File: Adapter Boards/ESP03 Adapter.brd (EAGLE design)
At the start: 30.1 x 19 mm, 3 parts, among them U1 ESP03

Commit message: Added OSHW logos
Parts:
- added LOGO1: OSHW-LOGOM, SparkFun-Aesthetics:OSHW-LOGO-M
- renumbered JP1 to 1, JP2 to 2
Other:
- board size 30.1 x 19 mm -> 30.1 x 19.7 mm
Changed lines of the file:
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@@
 <plain>
 <wire x1="0" y1="0" x2="30.15" y2="0" width="0" layer="20"/>
-<wire x1="30.15" y1="0" x2="30.15" y2="19.04" width="0" layer="20"/>
-<wire x1="30.15" y1="19.04" x2="0" y2="19.04" width="0" layer="20"/>
-<wire x1="0" y1="19.04" x2="0" y2="0" width="0" layer="20"/>
+<wire x1="30.15" y1="0" x2="30.15" y2="19.675" width="0" layer="20"/>
+<wire x1="30.15" y1="19.675" x2="0" y2="19.675" width="0" layer="20"/>
+<wire x1="0" y1="19.675" x2="0" y2="0" width="0" layer="20"/>
 </plain>
 <attributes>
@@
 </autorouter>
 <elements>
-<element name="JP1" library="SparkFun-Connectors" package="1X07" value="" x="1.905" y="1.905" rot="R90"/>
-<element name="JP2" library="SparkFun-Connectors" package="1X07" value="" x="28.575" y="1.905" rot="R90"/>
+<element name="1" library="SparkFun-Connectors" package="1X07" value="" x="1.905" y="1.905" smashed="yes" rot="R90">
+<attribute name="NAME" x="3.7338" y="0.7112" size="1.27" layer="27" ratio="10" rot="R270"/>
+<attribute name="VALUE" x="5.08" y="0.635" size="1.27" layer="27" rot="R90"/>
+</element>
+<element name="2" library="SparkFun-Connectors" package="1X07" value="" x="28.575" y="1.905" smashed="yes" rot="R90">
+<attribute name="NAME" x="26.7462" y="0.5588" size="1.27" layer="27" ratio="10" rot="R90"/>
+<attribute name="VALUE" x="31.75" y="0.635" size="1.27" layer="27" rot="R90"/>
+</element>
 <element name="U1" library="ESP" package="ESP03" value="ESP03" x="8.89" y="18.415"/>
+<element name="LOGO1" library="SparkFun-Aesthetics" package="OSHW-LOGO-M" value="OSHW-LOGOM" x="24.13" y="16.51"/>
 </elements>
 <signals>
 <signal name="N$1">
 <contactref element="U1" pad="VCC"/>
-<contactref element="JP1" pad="7"/>
+<contactref element="1" pad="7"/>
 <wire x1="9.09" y1="14.015" x2="5.035" y2="14.015" width="0.4064" layer="1"/>
 <wire x1="5.035" y1="14.015" x2="1.905" y2="17.145" width="0.4064" layer="1"/>
@@
 <signal name="N$2">
 <contactref element="U1" pad="GPIO14"/>
-<contactref element="JP1" pad="6"/>
+<contactref element="1" pad="6"/>
 <wire x1="9.09" y1="12.015" x2="4.495" y2="12.015" width="0.4064" layer="1"/>
 <wire x1="4.495" y1="12.015" x2="1.905" y2="14.605" width="0.4064" layer="1"/>
@@
 <signal name="N$3">
 <contactref element="U1" pad="GPIO12"/>
-<contactref element="JP1" pad="5"/>
+<contactref element="1" pad="5"/>
 <wire x1="9.09" y1="10.015" x2="3.955" y2="10.015" width="0.4064" layer="1"/>
 <wire x1="3.955" y1="10.015" x2="1.905" y2="12.065" width="0.4064" layer="1"/>
@@
 <signal name="N$4">
 <contactref element="U1" pad="GPIO13"/>
-<contactref element="JP1" pad="4"/>
+<contactref element="1" pad="4"/>
 <wire x1="9.09" y1="8.015" x2="3.415" y2="8.015" width="0.4064" layer="1"/>
 <wire x1="3.415" y1="8.015" x2="1.905" y2="9.525" width="0.4064" layer="1"/>
@@
 <signal name="N$5">
 <contactref element="U1" pad="GPIO15"/>
-<contactref element="JP1" pad="3"/>
+<contactref element="1" pad="3"/>
 <wire x1="9.09" y1="6.015" x2="2.875" y2="6.015" width="0.4064" layer="1"/>
 <wire x1="2.875" y1="6.015" x2="1.905" y2="6.985" width="0.4064" layer="1"/>
@@
 <signal name="N$6">
 <contactref element="U1" pad="GPIO2"/>
-<contactref element="JP1" pad="2"/>
+<contactref element="1" pad="2"/>
 <wire x1="9.09" y1="4.015" x2="2.335" y2="4.015" width="0.4064" layer="1"/>
 <wire x1="2.335" y1="4.015" x2="1.905" y2="4.445" width="0.4064" layer="1"/>
@@
 <signal name="N$7">
 <contactref element="U1" pad="GPIO0"/>
-<contactref element="JP1" pad="1"/>
+<contactref element="1" pad="1"/>
 <wire x1="9.09" y1="2.015" x2="2.015" y2="2.015" width="0.4064" layer="1"/>
 <wire x1="2.015" y1="2.015" x2="1.905" y2="1.905" width="0.4064" layer="1"/>
@@
 <signal name="N$8">
 <contactref element="U1" pad="ANT"/>
-<contactref element="JP2" pad="7"/>
+<contactref element="2" pad="7"/>
 <wire x1="20.69" y1="14.015" x2="25.445" y2="14.015" width="0.4064" layer="1"/>
 <wire x1="25.445" y1="14.015" x2="28.575" y2="17.145" width="0.4064" layer="1"/>
@@
 <signal name="N$9">
 <contactref element="U1" pad="CH_PD"/>
-<contactref element="JP2" pad="6"/>
+<contactref element="2" pad="6"/>
 <wire x1="20.69" y1="12.015" x2="25.985" y2="12.015" width="0.4064" layer="1"/>
 <wire x1="25.985" y1="12.015" x2="28.575" y2="14.605" width="0.4064" layer="1"/>
@@
 <signal name="N$10">
 <contactref element="U1" pad="GPIO18"/>
-<contactref element="JP2" pad="5"/>
+<contactref element="2" pad="5"/>
 <wire x1="20.69" y1="10.015" x2="26.525" y2="10.015" width="0.4064" layer="1"/>
 <wire x1="26.525" y1="10.015" x2="28.575" y2="12.065" width="0.4064" layer="1"/>
@@
 <signal name="N$11">
 <contactref element="U1" pad="URXD"/>
-<contactref element="JP2" pad="4"/>
+<contactref element="2" pad="4"/>
 <wire x1="20.69" y1="8.015" x2="27.065" y2="8.015" width="0.4064" layer="1"/>
 <wire x1="27.065" y1="8.015" x2="28.575" y2="9.525" width="0.4064" layer="1"/>
@@
 <signal name="N$12">
 <contactref element="U1" pad="UTXD"/>
-<contactref element="JP2" pad="3"/>
+<contactref element="2" pad="3"/>
 <wire x1="20.69" y1="6.015" x2="27.605" y2="6.015" width="0.4064" layer="1"/>
 <wire x1="27.605" y1="6.015" x2="28.575" y2="6.985" width="0.4064" layer="1"/>
@@
 <signal name="N$13">
 <contactref element="U1" pad="GND"/>
-<contactref element="JP2" pad="1"/>
+<contactref element="2" pad="1"/>
 <wire x1="20.69" y1="2.015" x2="28.465" y2="2.015" width="0.4064" layer="1"/>
 <wire x1="28.465" y1="2.015" x2="28.575" y2="1.905" width="0.4064" layer="1"/>

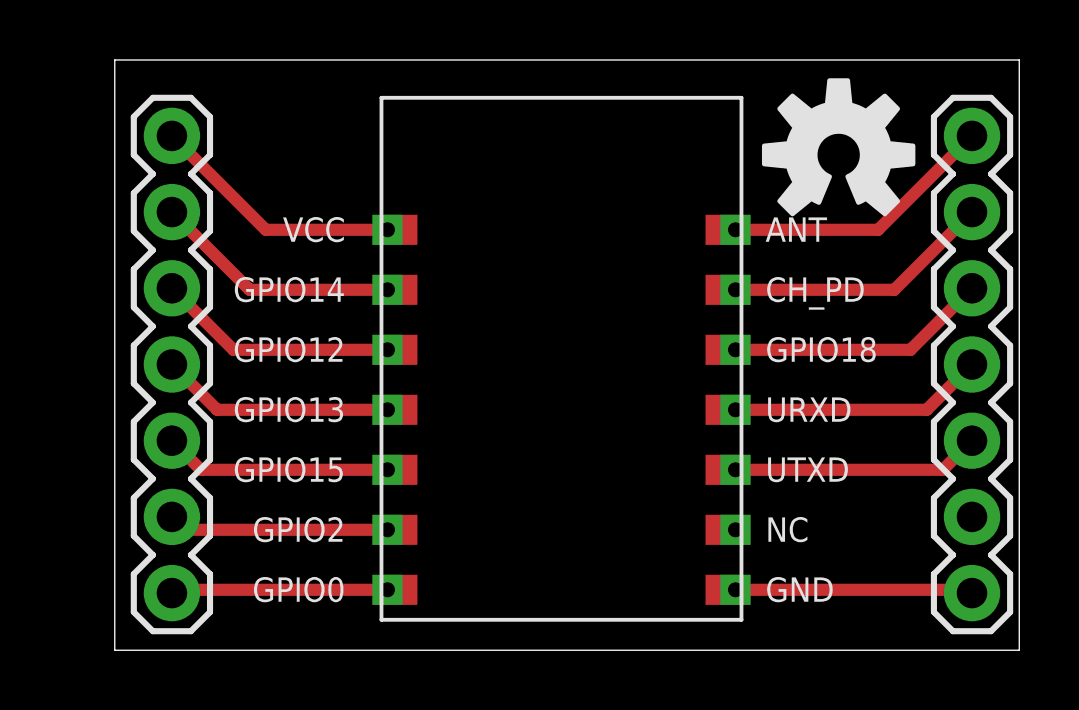
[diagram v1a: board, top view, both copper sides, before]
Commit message: Added hark logo
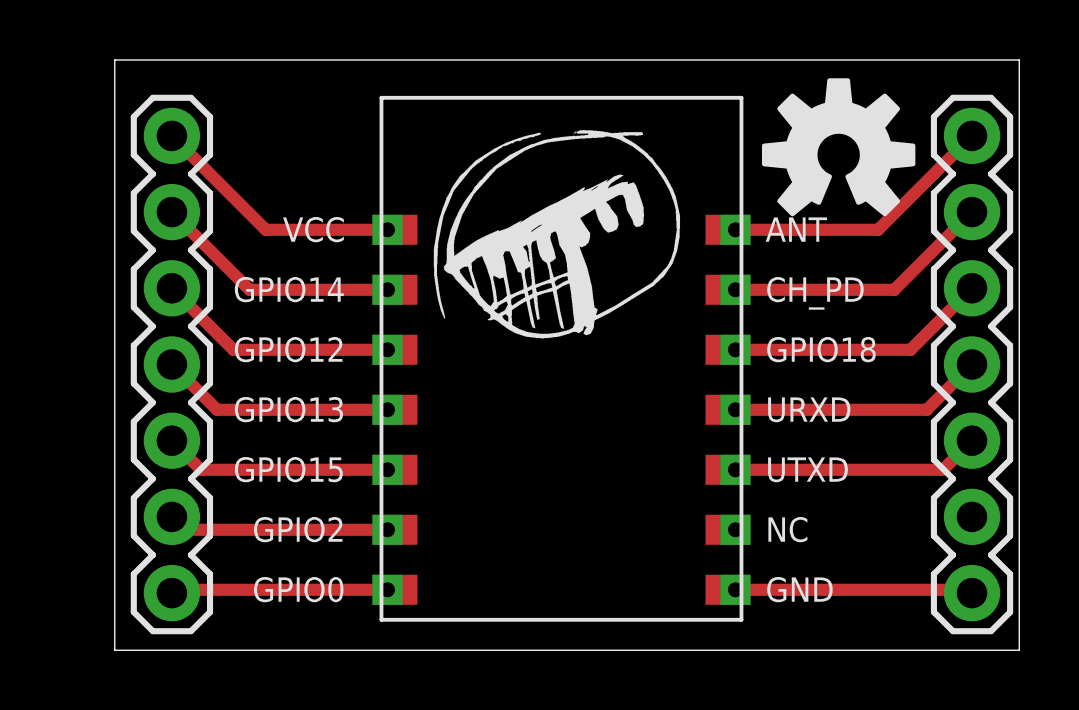
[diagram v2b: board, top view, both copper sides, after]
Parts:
- added U$1: (no value), ESP:HARK
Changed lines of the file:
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@@
 <layer number="25" name="tNames" color="7" fill="1" visible="yes" active="yes"/>
 <layer number="26" name="bNames" color="7" fill="1" visible="yes" active="yes"/>
-<layer number="27" name="tValues" color="7" fill="1" visible="yes" active="yes"/>
-<layer number="28" name="bValues" color="7" fill="1" visible="yes" active="yes"/>
+<layer number="27" name="tValues" color="7" fill="1" visible="no" active="yes"/>
+<layer number="28" name="bValues" color="7" fill="1" visible="no" active="yes"/>
 <layer number="29" name="tStop" color="7" fill="3" visible="no" active="yes"/>
 <layer number="30" name="bStop" color="7" fill="6" visible="no" active="yes"/>
@@
 <element name="U1" library="ESP" package="ESP03" value="ESP03" x="8.89" y="18.415"/>
 <element name="LOGO1" library="SparkFun-Aesthetics" package="OSHW-LOGO-M" value="OSHW-LOGOM" x="24.13" y="16.51"/>
+<element name="U$1" library="ESP" package="HARK" value="" x="10.16" y="10.16"/>
 </elements>
 <signals>

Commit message: Micronise hark logo; add multiple sizes
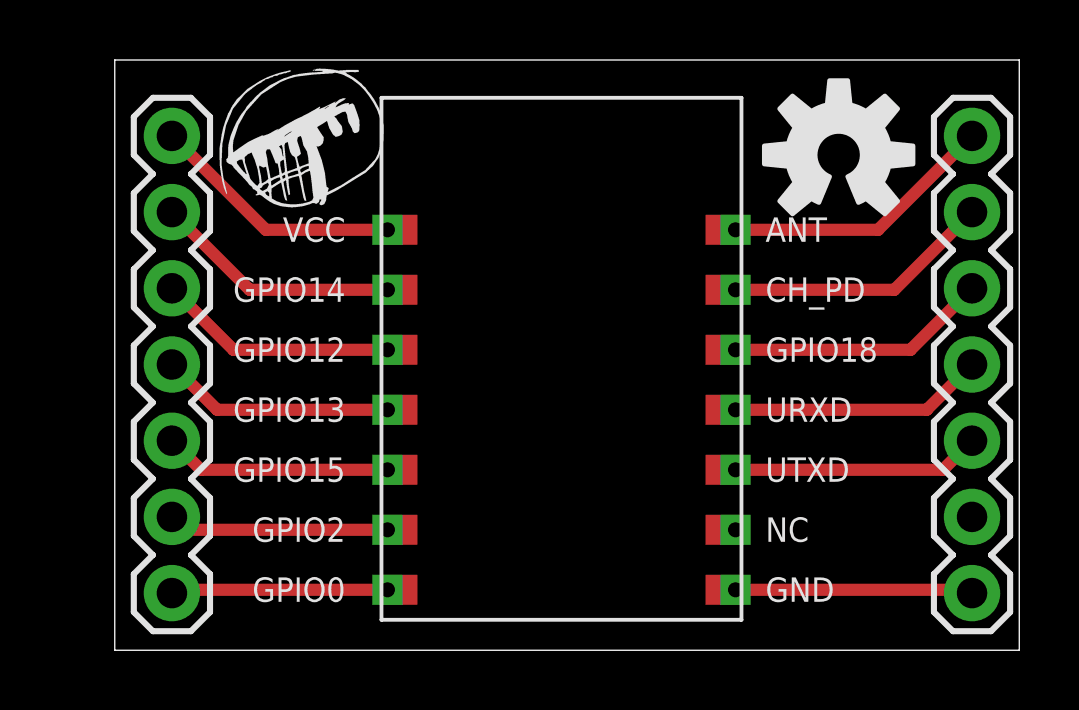
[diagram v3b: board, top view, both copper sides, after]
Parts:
- removed U$1: (no value), ESP:HARK
- added E$1: (no value), ESP:HARK-S
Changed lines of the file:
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@@
 <element name="U1" library="ESP" package="ESP03" value="ESP03" x="8.89" y="18.415"/>
 <element name="LOGO1" library="SparkFun-Aesthetics" package="OSHW-LOGO-M" value="OSHW-LOGOM" x="24.13" y="16.51"/>
-<element name="U$1" library="ESP" package="HARK" value="" x="10.16" y="10.16"/>
+<element name="E$1" library="ESP" package="HARK-S" value="" x="3.175" y="14.605"/>
 </elements>
 <signals>

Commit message: Repair pads; resize ESP12
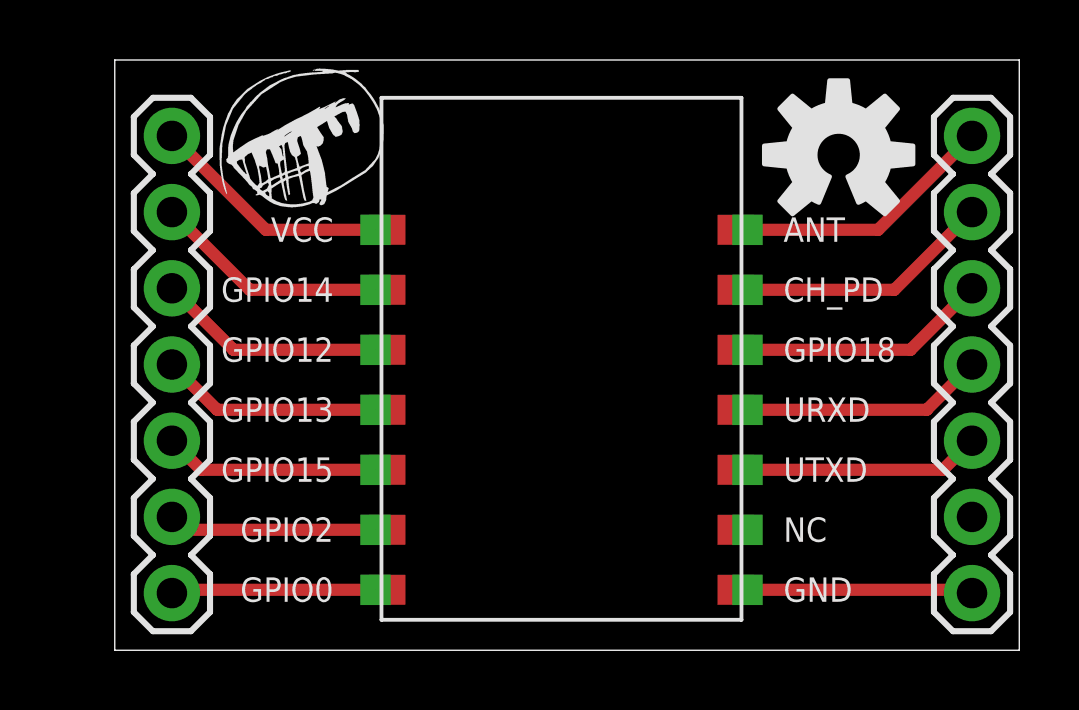
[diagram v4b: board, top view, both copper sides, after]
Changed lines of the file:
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@@
 <contactref element="U1" pad="VCC"/>
 <contactref element="1" pad="7"/>
-<wire x1="9.09" y1="14.015" x2="5.035" y2="14.015" width="0.4064" layer="1"/>
+<wire x1="8.69" y1="14.015" x2="5.035" y2="14.015" width="0.4064" layer="1"/>
 <wire x1="5.035" y1="14.015" x2="1.905" y2="17.145" width="0.4064" layer="1"/>
 </signal>
@@
 <contactref element="U1" pad="GPIO14"/>
 <contactref element="1" pad="6"/>
-<wire x1="9.09" y1="12.015" x2="4.495" y2="12.015" width="0.4064" layer="1"/>
+<wire x1="8.69" y1="12.015" x2="4.495" y2="12.015" width="0.4064" layer="1"/>
 <wire x1="4.495" y1="12.015" x2="1.905" y2="14.605" width="0.4064" layer="1"/>
 </signal>
@@
 <contactref element="U1" pad="GPIO12"/>
 <contactref element="1" pad="5"/>
-<wire x1="9.09" y1="10.015" x2="3.955" y2="10.015" width="0.4064" layer="1"/>
+<wire x1="8.69" y1="10.015" x2="3.955" y2="10.015" width="0.4064" layer="1"/>
 <wire x1="3.955" y1="10.015" x2="1.905" y2="12.065" width="0.4064" layer="1"/>
 </signal>
@@
 <contactref element="U1" pad="GPIO13"/>
 <contactref element="1" pad="4"/>
-<wire x1="9.09" y1="8.015" x2="3.415" y2="8.015" width="0.4064" layer="1"/>
+<wire x1="8.69" y1="8.015" x2="3.415" y2="8.015" width="0.4064" layer="1"/>
 <wire x1="3.415" y1="8.015" x2="1.905" y2="9.525" width="0.4064" layer="1"/>
 </signal>
@@
 <contactref element="U1" pad="GPIO15"/>
 <contactref element="1" pad="3"/>
-<wire x1="9.09" y1="6.015" x2="2.875" y2="6.015" width="0.4064" layer="1"/>
+<wire x1="8.69" y1="6.015" x2="2.875" y2="6.015" width="0.4064" layer="1"/>
 <wire x1="2.875" y1="6.015" x2="1.905" y2="6.985" width="0.4064" layer="1"/>
 </signal>
@@
 <contactref element="U1" pad="GPIO2"/>
 <contactref element="1" pad="2"/>
-<wire x1="9.09" y1="4.015" x2="2.335" y2="4.015" width="0.4064" layer="1"/>
+<wire x1="8.69" y1="4.015" x2="2.335" y2="4.015" width="0.4064" layer="1"/>
 <wire x1="2.335" y1="4.015" x2="1.905" y2="4.445" width="0.4064" layer="1"/>
 </signal>
@@
 <contactref element="U1" pad="GPIO0"/>
 <contactref element="1" pad="1"/>
-<wire x1="9.09" y1="2.015" x2="2.015" y2="2.015" width="0.4064" layer="1"/>
+<wire x1="8.69" y1="2.015" x2="2.015" y2="2.015" width="0.4064" layer="1"/>
 <wire x1="2.015" y1="2.015" x2="1.905" y2="1.905" width="0.4064" layer="1"/>
 </signal>
@@
 <contactref element="U1" pad="ANT"/>
 <contactref element="2" pad="7"/>
-<wire x1="20.69" y1="14.015" x2="25.445" y2="14.015" width="0.4064" layer="1"/>
+<wire x1="21.09" y1="14.015" x2="25.445" y2="14.015" width="0.4064" layer="1"/>
 <wire x1="25.445" y1="14.015" x2="28.575" y2="17.145" width="0.4064" layer="1"/>
 </signal>
@@
 <contactref element="U1" pad="CH_PD"/>
 <contactref element="2" pad="6"/>
-<wire x1="20.69" y1="12.015" x2="25.985" y2="12.015" width="0.4064" layer="1"/>
+<wire x1="21.09" y1="12.015" x2="25.985" y2="12.015" width="0.4064" layer="1"/>
 <wire x1="25.985" y1="12.015" x2="28.575" y2="14.605" width="0.4064" layer="1"/>
 </signal>
@@
 <contactref element="U1" pad="GPIO18"/>
 <contactref element="2" pad="5"/>
-<wire x1="20.69" y1="10.015" x2="26.525" y2="10.015" width="0.4064" layer="1"/>
+<wire x1="21.09" y1="10.015" x2="26.525" y2="10.015" width="0.4064" layer="1"/>
 <wire x1="26.525" y1="10.015" x2="28.575" y2="12.065" width="0.4064" layer="1"/>
 </signal>
@@
 <contactref element="U1" pad="URXD"/>
 <contactref element="2" pad="4"/>
-<wire x1="20.69" y1="8.015" x2="27.065" y2="8.015" width="0.4064" layer="1"/>
+<wire x1="21.09" y1="8.015" x2="27.065" y2="8.015" width="0.4064" layer="1"/>
 <wire x1="27.065" y1="8.015" x2="28.575" y2="9.525" width="0.4064" layer="1"/>
 </signal>
@@
 <contactref element="U1" pad="UTXD"/>
 <contactref element="2" pad="3"/>
-<wire x1="20.69" y1="6.015" x2="27.605" y2="6.015" width="0.4064" layer="1"/>
+<wire x1="21.09" y1="6.015" x2="27.605" y2="6.015" width="0.4064" layer="1"/>
 <wire x1="27.605" y1="6.015" x2="28.575" y2="6.985" width="0.4064" layer="1"/>
 </signal>
@@
 <contactref element="U1" pad="GND"/>
 <contactref element="2" pad="1"/>
-<wire x1="20.69" y1="2.015" x2="28.465" y2="2.015" width="0.4064" layer="1"/>
+<wire x1="21.09" y1="2.015" x2="28.465" y2="2.015" width="0.4064" layer="1"/>
 <wire x1="28.465" y1="2.015" x2="28.575" y2="1.905" width="0.4064" layer="1"/>
 </signal>
